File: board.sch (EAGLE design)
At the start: 8 parts

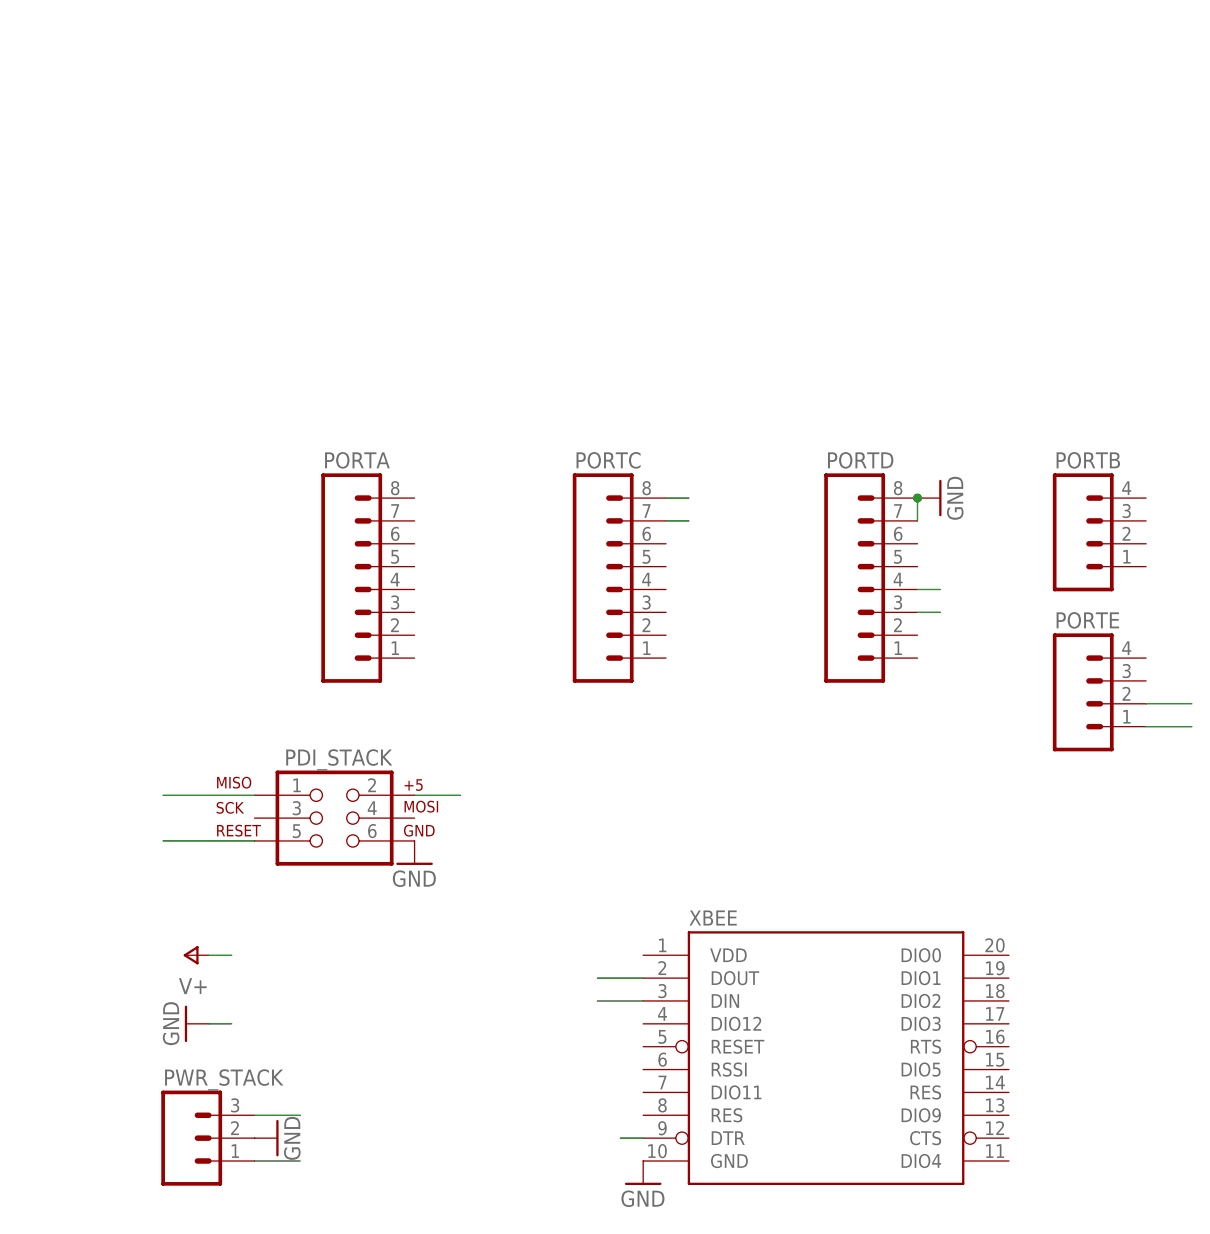
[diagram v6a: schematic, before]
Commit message: we have 6 HW pwm-channels, so add that many dual-mosfets
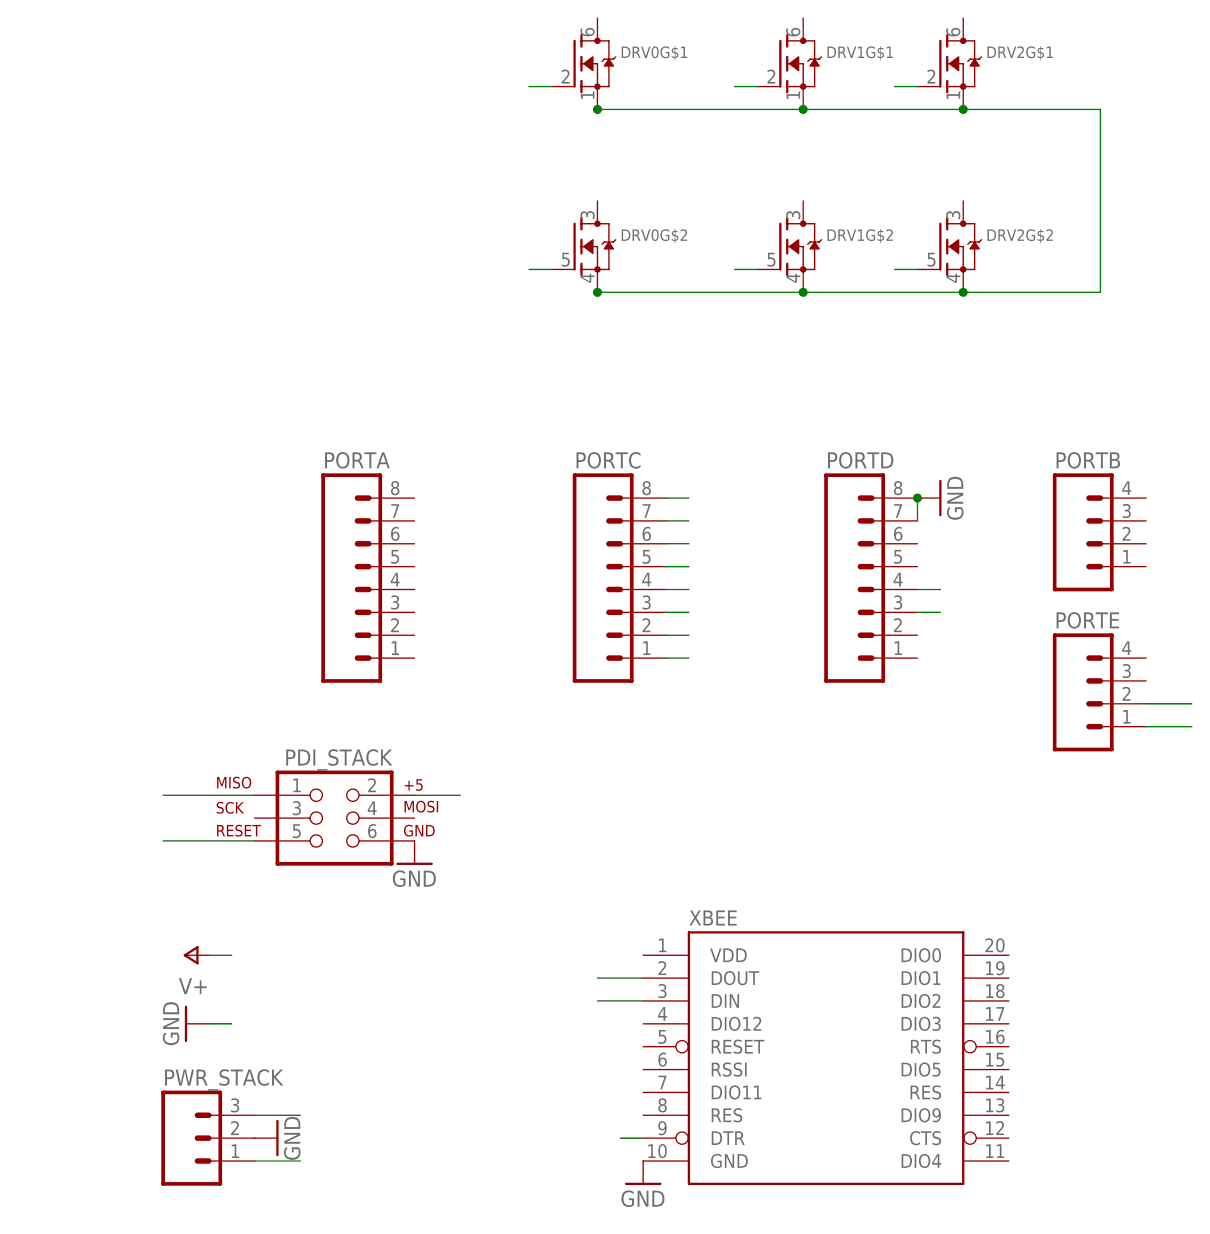
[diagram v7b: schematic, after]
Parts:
- added DRV0, DRV1, DRV2: (no value), microbuilder:MOSFET-N_DUAL
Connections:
- new net GND_PWR: DRV0G$1.S, DRV0G$2.S, DRV1G$1.S, DRV1G$2.S, DRV2G$1.S, DRV2G$2.S
- new net PWM0: DRV0G$1.G, PORTC.1
- new net PWM1: DRV0G$2.G, PORTC.2
- new net PWM2: DRV1G$1.G, PORTC.3
- new net PWM3: DRV1G$2.G, PORTC.4
- new net PWM4: DRV2G$1.G, PORTC.5
- new net PWM5: DRV2G$2.G, PORTC.6
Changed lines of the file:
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@@
 <layer number="106" name="bPlate" color="7" fill="1" visible="no" active="yes"/>
 <layer number="107" name="Crop" color="7" fill="1" visible="no" active="yes"/>
+<layer number="108" name="tBridges" color="7" fill="1" visible="yes" active="yes"/>
+<layer number="109" name="tBPL" color="7" fill="1" visible="yes" active="yes"/>
+<layer number="110" name="bBPL" color="7" fill="1" visible="yes" active="yes"/>
+<layer number="111" name="MPL" color="7" fill="1" visible="yes" active="yes"/>
+<layer number="112" name="tSilk" color="7" fill="1" visible="yes" active="yes"/>
 <layer number="116" name="Patch_BOT" color="9" fill="4" visible="no" active="yes"/>
 <layer number="121" name="_tsilk" color="7" fill="1" visible="no" active="yes"/>
 <layer number="122" name="_bsilk" color="7" fill="1" visible="no" active="yes"/>
 <layer number="125" name="_tNames" color="7" fill="1" visible="no" active="yes"/>
+<layer number="126" name="_bNames" color="7" fill="1" visible="yes" active="yes"/>
+<layer number="127" name="_tValues" color="7" fill="1" visible="yes" active="yes"/>
+<layer number="128" name="_bValues" color="7" fill="1" visible="yes" active="yes"/>
 <layer number="144" name="Drill_legend" color="7" fill="1" visible="no" active="yes"/>
 <layer number="151" name="HeatSink" color="7" fill="1" visible="no" active="yes"/>
+<layer number="152" name="_bDocu" color="7" fill="1" visible="yes" active="yes"/>
 <layer number="199" name="Contour" color="7" fill="1" visible="yes" active="yes"/>
 <layer number="200" name="200bmp" color="1" fill="10" visible="no" active="yes"/>
@@
 <layer number="223" name="223bmp" color="24" fill="1" visible="no" active="no"/>
 <layer number="224" name="224bmp" color="25" fill="1" visible="no" active="no"/>
+<layer number="248" name="Housing" color="7" fill="1" visible="yes" active="yes"/>
+<layer number="249" name="Edge" color="7" fill="1" visible="yes" active="yes"/>
 <layer number="250" name="Descript" color="3" fill="1" visible="no" active="no"/>
 <layer number="251" name="SMDround" color="12" fill="11" visible="no" active="no"/>
@@
 <classes>
 <class number="0" name="default" width="0" drill="0">
+</class>
+<class number="1" name="PWR" width="0.4064" drill="0">
 </class>
 </classes>
@@
 <part name="PWR_STACK" library="SparkFun-Connectors" deviceset="M03" device="PTH"/>
 <part name="GND5" library="supply1" deviceset="GND" device=""/>
+<part name="DRV0" library="microbuilder" deviceset="MOSFET-N_DUAL" device=""/>
+<part name="DRV1" library="microbuilder" deviceset="MOSFET-N_DUAL" device=""/>
+<part name="DRV2" library="microbuilder" deviceset="MOSFET-N_DUAL" device=""/>
 </parts>
 <sheets>
@@
 <instance part="PWR_STACK" gate="G$1" x="-2.54" y="35.56"/>
 <instance part="GND5" gate="1" x="7.62" y="35.56" rot="R90"/>
+<instance part="DRV0" gate="G$1" x="40.64" y="154.94"/>
+<instance part="DRV0" gate="G$2" x="40.64" y="134.62"/>
+<instance part="DRV1" gate="G$1" x="63.5" y="154.94"/>
+<instance part="DRV1" gate="G$2" x="63.5" y="134.62"/>
+<instance part="DRV2" gate="G$1" x="81.28" y="154.94"/>
+<instance part="DRV2" gate="G$2" x="81.28" y="134.62"/>
 </instances>
 <busses>
 </busses>
 <nets>
-<net name="GND" class="0">
+<net name="GND" class="1">
 <segment>
 <pinref part="PORTD" gate="G$1" pin="7"/>
@@
 </segment>
 </net>
-<net name="VBAT" class="0">
+<net name="VBAT" class="1">
 <segment>
 <pinref part="P+1" gate="1" pin="V+"/>
@@
 </segment>
 </net>
+<net name="GND_PWR" class="1">
+<segment>
+<pinref part="DRV0" gate="G$1" pin="S"/>
+<wire x1="43.18" y1="149.86" x2="66.04" y2="149.86" width="0.1524" layer="91"/>
+<wire x1="66.04" y1="149.86" x2="83.82" y2="149.86" width="0.1524" layer="91"/>
+<wire x1="83.82" y1="149.86" x2="99.06" y2="149.86" width="0.1524" layer="91"/>
+<wire x1="99.06" y1="149.86" x2="99.06" y2="129.54" width="0.1524" layer="91"/>
+<pinref part="DRV0" gate="G$2" pin="S"/>
+<wire x1="99.06" y1="129.54" x2="83.82" y2="129.54" width="0.1524" layer="91"/>
+<pinref part="DRV1" gate="G$2" pin="S"/>
+<wire x1="83.82" y1="129.54" x2="66.04" y2="129.54" width="0.1524" layer="91"/>
+<wire x1="66.04" y1="129.54" x2="43.18" y2="129.54" width="0.1524" layer="91"/>
+<junction x="66.04" y="129.54"/>
+<pinref part="DRV2" gate="G$2" pin="S"/>
+<junction x="83.82" y="129.54"/>
+<pinref part="DRV2" gate="G$1" pin="S"/>
+<junction x="83.82" y="149.86"/>
+<pinref part="DRV1" gate="G$1" pin="S"/>
+<junction x="66.04" y="149.86"/>
+<junction x="43.18" y="149.86"/>
+<junction x="43.18" y="129.54"/>
+</segment>
+</net>
+<net name="PWM0" class="0">
+<segment>
+<pinref part="PORTC" gate="G$1" pin="1"/>
+<wire x1="50.8" y1="88.9" x2="53.34" y2="88.9" width="0.1524" layer="91"/>
+</segment>
+<segment>
+<pinref part="DRV0" gate="G$1" pin="G"/>
+<wire x1="38.1" y1="152.4" x2="35.56" y2="152.4" width="0.1524" layer="91"/>
+</segment>
+</net>
+<net name="PWM1" class="0">
+<segment>
+<pinref part="PORTC" gate="G$1" pin="2"/>
+<wire x1="50.8" y1="91.44" x2="53.34" y2="91.44" width="0.1524" layer="91"/>
+</segment>
+<segment>
+<pinref part="DRV0" gate="G$2" pin="G"/>
+<wire x1="38.1" y1="132.08" x2="35.56" y2="132.08" width="0.1524" layer="91"/>
+</segment>
+</net>
+<net name="PWM2" class="0">
+<segment>
+<pinref part="PORTC" gate="G$1" pin="3"/>
+<wire x1="50.8" y1="93.98" x2="53.34" y2="93.98" width="0.1524" layer="91"/>
+</segment>
+<segment>
+<pinref part="DRV1" gate="G$1" pin="G"/>
+<wire x1="60.96" y1="152.4" x2="58.42" y2="152.4" width="0.1524" layer="91"/>
+</segment>
+</net>
+<net name="PWM3" class="0">
+<segment>
+<pinref part="PORTC" gate="G$1" pin="4"/>
+<wire x1="50.8" y1="96.52" x2="53.34" y2="96.52" width="0.1524" layer="91"/>
+</segment>
+<segment>
+<pinref part="DRV1" gate="G$2" pin="G"/>
+<wire x1="60.96" y1="132.08" x2="58.42" y2="132.08" width="0.1524" layer="91"/>
+</segment>
+</net>
+<net name="PWM4" class="0">
+<segment>
+<pinref part="PORTC" gate="G$1" pin="5"/>
+<wire x1="50.8" y1="99.06" x2="53.34" y2="99.06" width="0.1524" layer="91"/>
+</segment>
+<segment>
+<pinref part="DRV2" gate="G$1" pin="G"/>
+<wire x1="78.74" y1="152.4" x2="76.2" y2="152.4" width="0.1524" layer="91"/>
+</segment>
+</net>
+<net name="PWM5" class="0">
+<segment>
+<pinref part="PORTC" gate="G$1" pin="6"/>
+<wire x1="50.8" y1="101.6" x2="53.34" y2="101.6" width="0.1524" layer="91"/>
+</segment>
+<segment>
+<pinref part="DRV2" gate="G$2" pin="G"/>
+<wire x1="78.74" y1="132.08" x2="76.2" y2="132.08" width="0.1524" layer="91"/>
+</segment>
+</net>

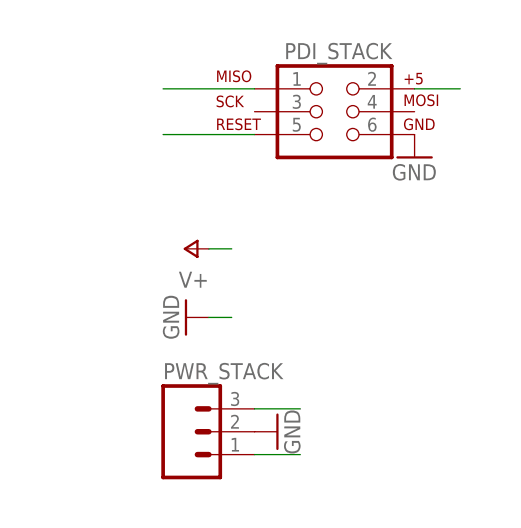
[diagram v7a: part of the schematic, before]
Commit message: added JST battery connector, alternatively 2.54mm pin header can be used
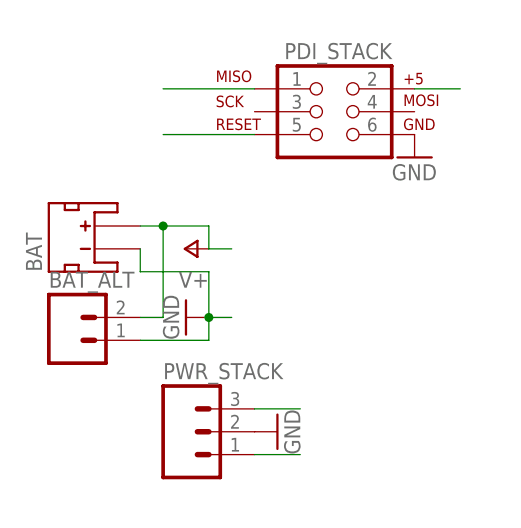
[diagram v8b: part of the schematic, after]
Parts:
- added BAT: (no value), SparkFun-Connectors:JST_2MM_MALE
- added BAT_ALT: (no value), SparkFun-Connectors:M02PTH
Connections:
- new net VBAT: BAT.+, BAT_ALT.2
- net GND: now also BAT.-, BAT_ALT.1
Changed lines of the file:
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@@
 <part name="DRV1" library="microbuilder" deviceset="MOSFET-N_DUAL" device=""/>
 <part name="DRV2" library="microbuilder" deviceset="MOSFET-N_DUAL" device=""/>
+<part name="BAT" library="SparkFun-Connectors" deviceset="JST_2MM_MALE" device=""/>
+<part name="BAT_ALT" library="SparkFun-Connectors" deviceset="M02" device="PTH"/>
 </parts>
 <sheets>
@@
 <instance part="DRV2" gate="G$1" x="81.28" y="154.94"/>
 <instance part="DRV2" gate="G$2" x="81.28" y="134.62"/>
+<instance part="BAT" gate="G$1" x="-12.7" y="55.88" rot="R90"/>
+<instance part="BAT_ALT" gate="G$1" x="-15.24" y="45.72"/>
 </instances>
 <busses>
@@
 <pinref part="GND3" gate="1" pin="GND"/>
 <wire x1="0" y1="48.26" x2="2.54" y2="48.26" width="0.1524" layer="91"/>
+<pinref part="BAT" gate="G$1" pin="-"/>
+<wire x1="-7.62" y1="55.88" x2="-7.62" y2="53.34" width="0.1524" layer="91"/>
+<wire x1="-7.62" y1="53.34" x2="0" y2="53.34" width="0.1524" layer="91"/>
+<wire x1="0" y1="53.34" x2="0" y2="48.26" width="0.1524" layer="91"/>
+<pinref part="BAT_ALT" gate="G$1" pin="1"/>
+<wire x1="-7.62" y1="45.72" x2="0" y2="45.72" width="0.1524" layer="91"/>
+<wire x1="0" y1="45.72" x2="0" y2="48.26" width="0.1524" layer="91"/>
+<junction x="0" y="48.26"/>
 </segment>
 <segment>
@@
 <pinref part="P+1" gate="1" pin="V+"/>
 <wire x1="0" y1="55.88" x2="2.54" y2="55.88" width="0.1524" layer="91"/>
+<pinref part="BAT" gate="G$1" pin="+"/>
+<wire x1="-7.62" y1="58.42" x2="-5.08" y2="58.42" width="0.1524" layer="91"/>
+<wire x1="-5.08" y1="58.42" x2="0" y2="58.42" width="0.1524" layer="91"/>
+<wire x1="0" y1="58.42" x2="0" y2="55.88" width="0.1524" layer="91"/>
+<pinref part="BAT_ALT" gate="G$1" pin="2"/>
+<wire x1="-7.62" y1="48.26" x2="-5.08" y2="48.26" width="0.1524" layer="91"/>
+<wire x1="-5.08" y1="48.26" x2="-5.08" y2="58.42" width="0.1524" layer="91"/>
+<junction x="-5.08" y="58.42"/>
 </segment>
 </net>
